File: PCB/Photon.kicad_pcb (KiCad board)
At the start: 2 copper layers, 21.2 x 74.4 mm, 44 parts, among them J1 USB_C_Receptacle_USB2.0_14P, J2 Conn_01x05_Socket, Q1 IRLML6402, Q2 IRLML6402, SW1 TS-1088-AR02016, U1 PY32F002AL15S6TU, U2 TP4056, U3 RT8059GJ5, U4 BCR421UW6-7, U5 DW01A, U6 FS8205A, U7 BCR421UW6-7

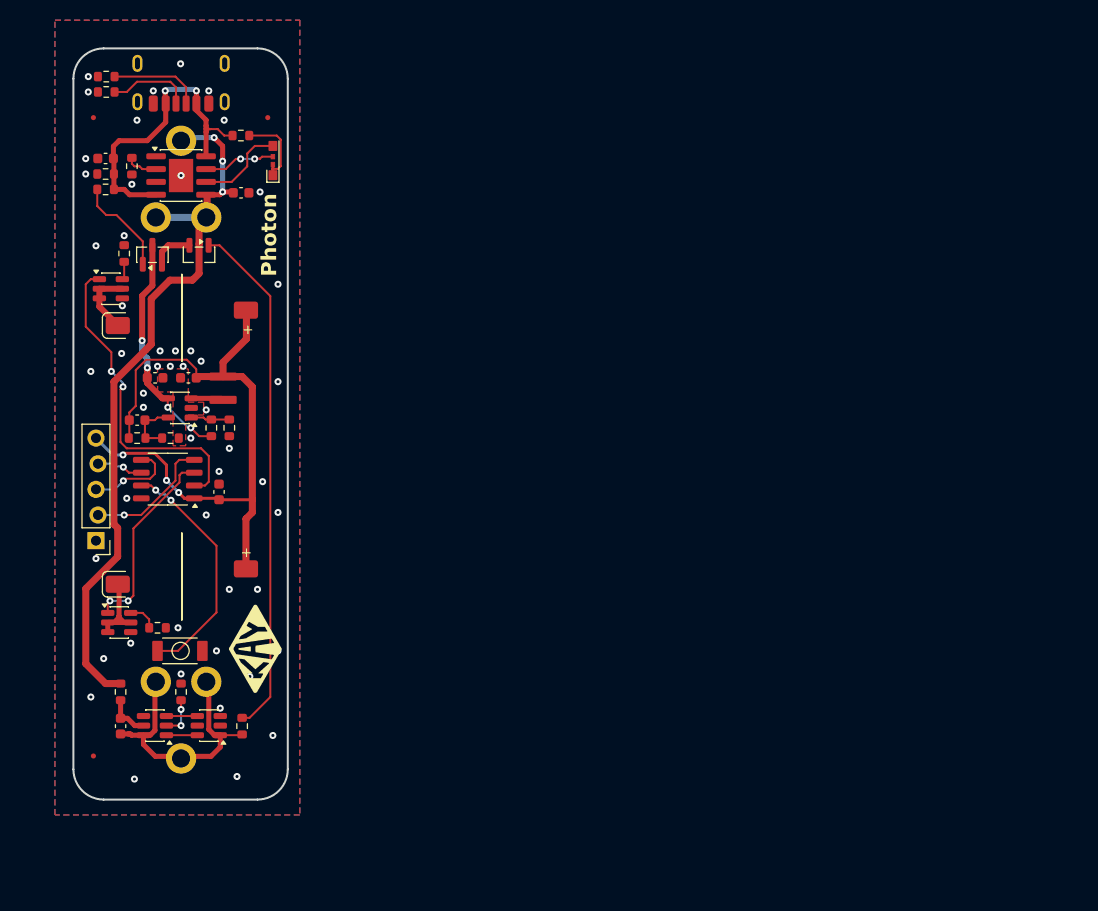
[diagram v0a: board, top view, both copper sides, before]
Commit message: Rotated PCB
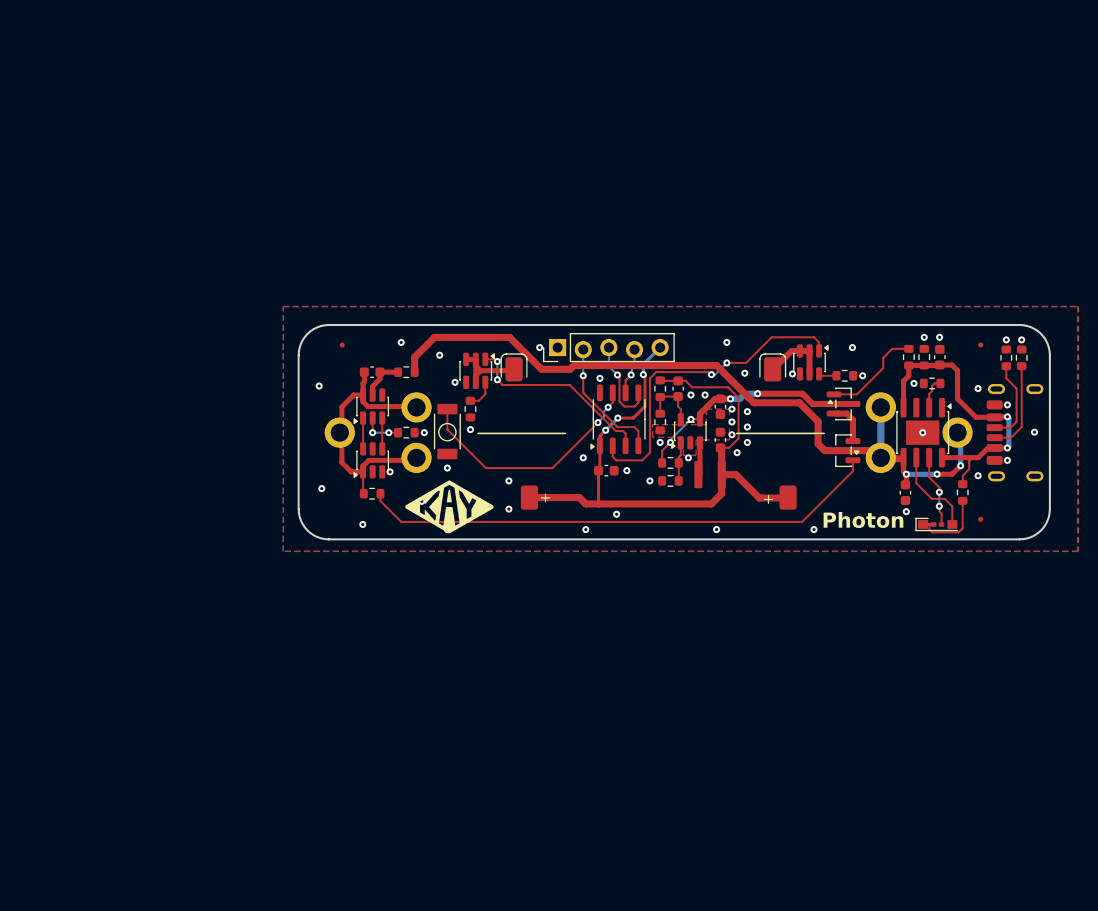
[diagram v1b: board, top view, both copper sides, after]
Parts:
- moved R1 94.9 mm to (136.2, 51.0), turned to 90 degrees
- moved R2 93.0 mm to (134.6, 51.0), turned to 90 degrees
- moved J1 91.1 mm to (136.7, 58.4), turned to 90 degrees
- moved FID3 90.7 mm to (132.1, 49.7), turned to -90 degrees
- moved C3 85.0 mm to (128.0, 50.9), turned to -90 degrees
- moved R5 83.1 mm to (126.5, 50.9), turned to 90 degrees
- moved R10 82.2 mm to (127.3, 53.5), turned to 180 degrees
- moved R4 81.3 mm to (125.0, 50.9), turned to -90 degrees
- moved FID1 81.1 mm to (132.1, 67.0), turned to -90 degrees
- moved BT1 80.1 mm to (125.2, 52.9), turned to 180 degrees
- moved R7 79.8 mm to (130.3, 64.3), turned to -90 degrees
- moved U2 77.8 mm to (126.4, 58.4), turned to -90 degrees
- moved D1 77.1 mm to (129.3, 67.5), turned to 180 degrees
- moved R13 72.4 mm to (118.6, 52.8), turned to 0 degrees
- moved C6 72.2 mm to (124.6, 64.3), turned to 90 degrees
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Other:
- board size 21.2 x 74.4 mm -> 74.4 x 21.2 mm

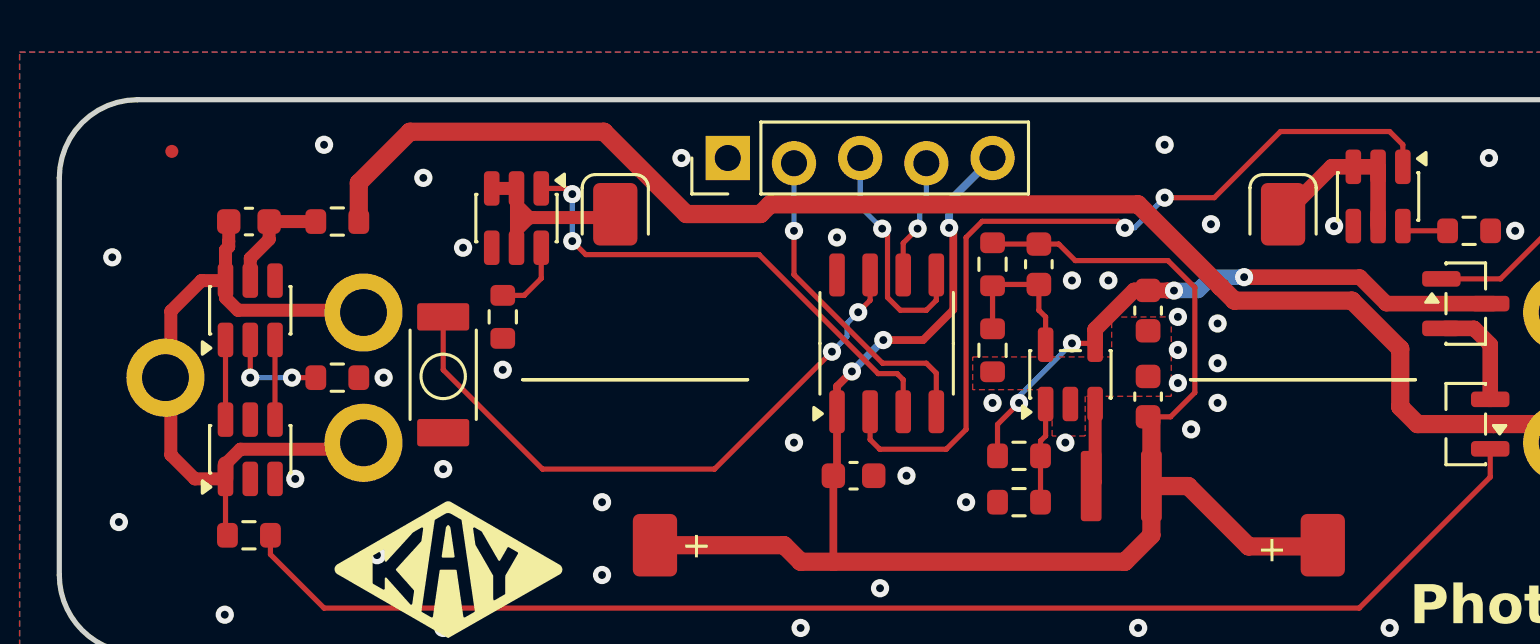
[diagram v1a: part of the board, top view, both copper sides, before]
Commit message: updated debug header and changed resistors for UVLO
Applied teardrop to all vias. some were missing. Thickened trace from neg battery terminal. Updated gerbers
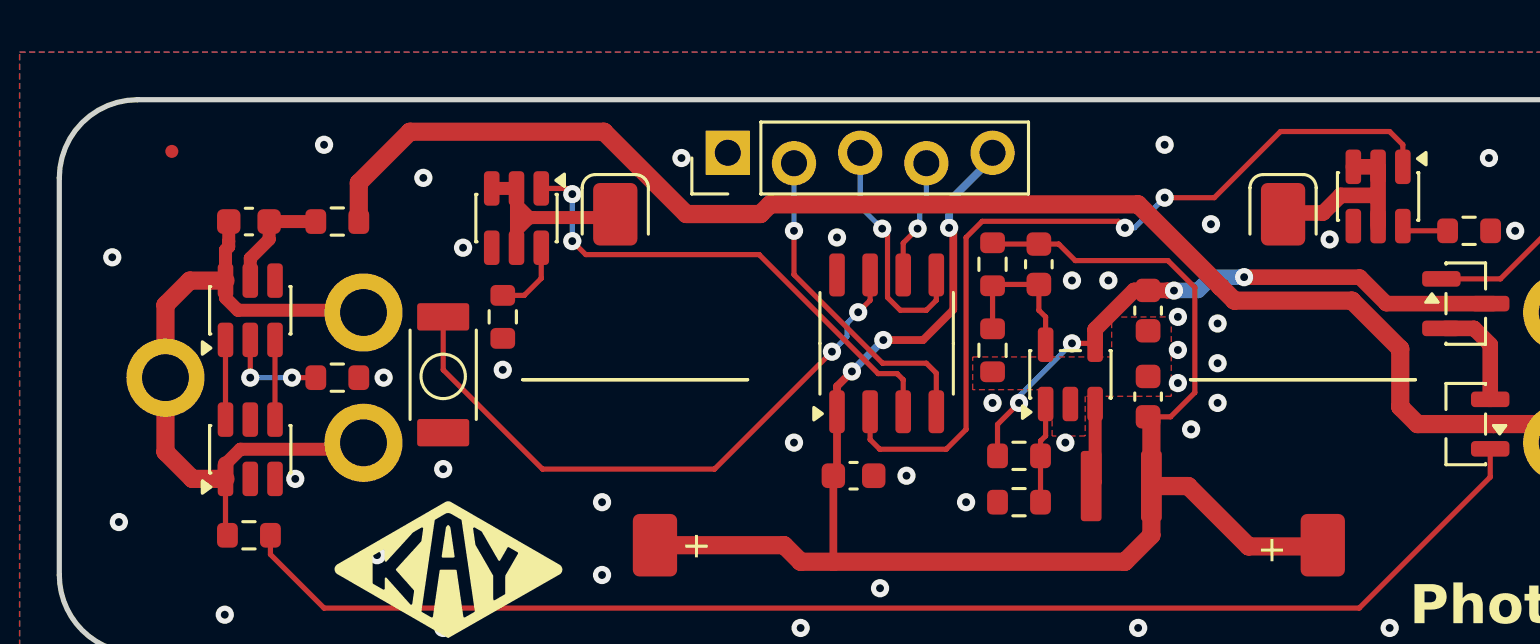
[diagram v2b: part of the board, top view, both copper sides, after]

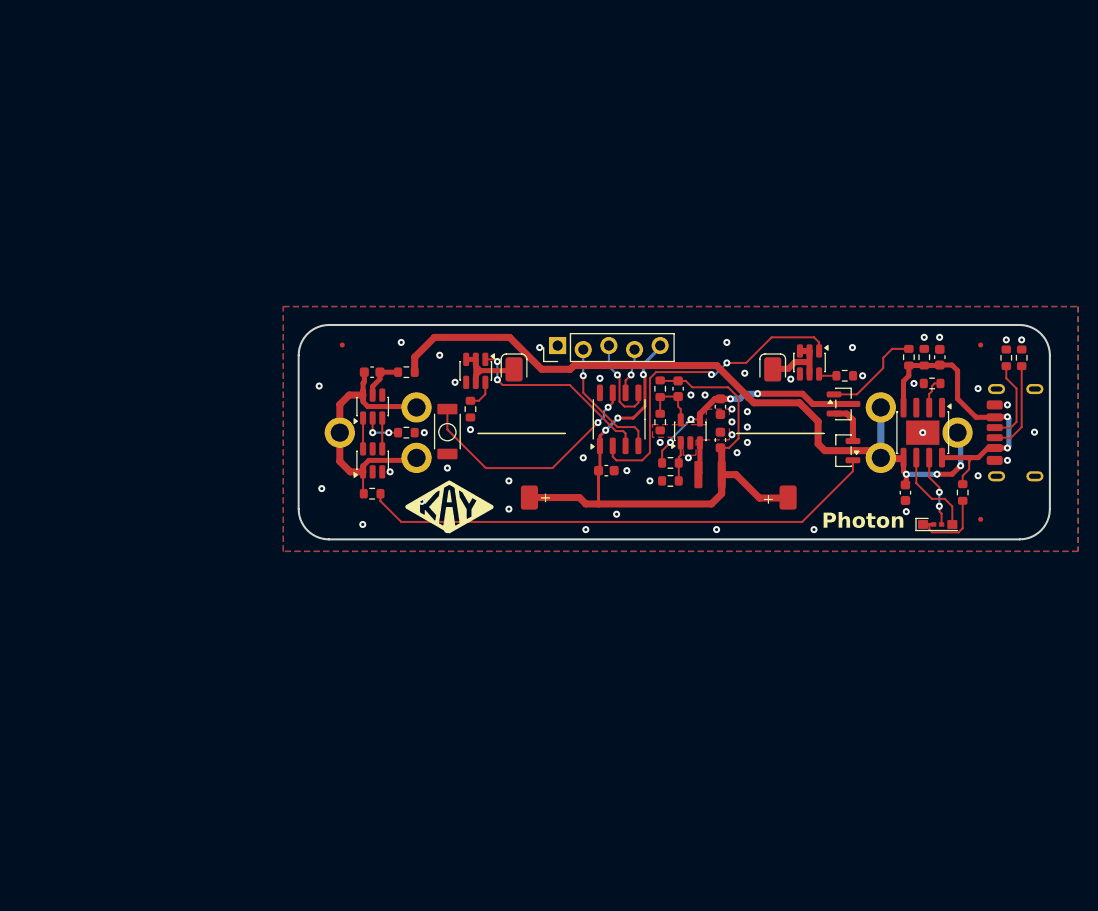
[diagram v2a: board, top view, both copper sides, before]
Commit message: switch to smt32 mcu and cleaned up pcb
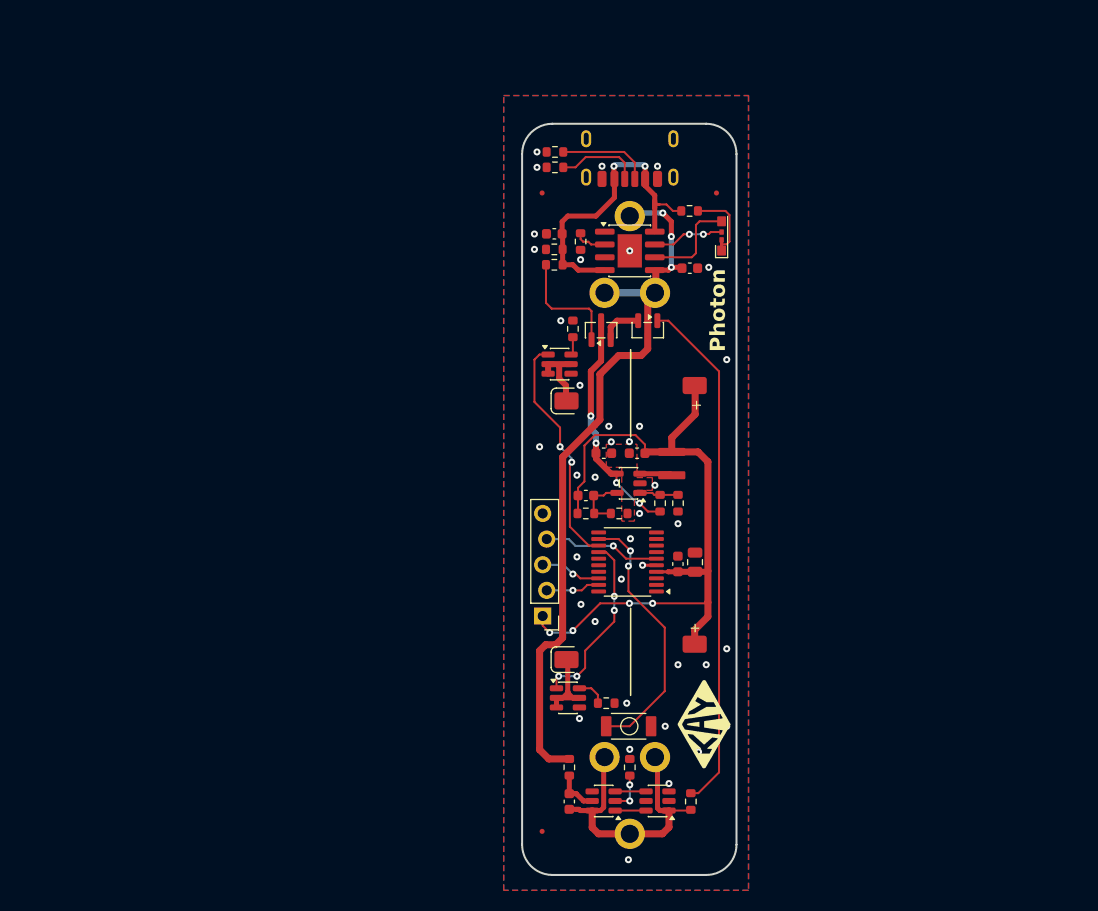
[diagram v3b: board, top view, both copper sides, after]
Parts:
- added C2: 100nF, Capacitor_SMD:C_0603_1608Metric, F.Cu at (102.1, 71.4)
- C1: value 100nF -> 4.7uF; footprint Capacitor_SMD:C_0603_1608Metric -> Capacitor_SMD:C_0805_2012Metric
- J1: value USB_C_Receptacle_USB2.0_14P -> USB_C_Receptacle_USB2.0_6P
- R5: renamed from R3; value 30K -> 12K
- R6: value 100K -> 10K
- U1: value PY32F002AL15S6TU -> STM32G030F6P6TR; footprint Package_SO:SOP-8_3.9x4.9mm_P1.27mm -> Package_SO:TSSOP-20_4.4x6.5mm_P0.65mm
- moved FID2 52.1 mm to (88.7, 97.9), turned to 0 degrees
- moved R1 50.5 mm to (89.9, 30.6), turned to 180 degrees
- moved R2 48.5 mm to (89.9, 32.1), turned to 180 degrees
- moved J1 48.5 mm to (97.3, 30.1), turned to 180 degrees
- moved C8 46.8 mm to (91.3, 94.9), turned to 90 degrees
- moved FID3 46.0 mm to (88.7, 34.6), turned to 0 degrees
- moved U4 45.3 mm to (94.7, 94.9), turned to 180 degrees
- moved U5 44.0 mm to (100.1, 94.9), turned to 180 degrees
- moved R14 43.9 mm to (103.4, 94.9), turned to 90 degrees
- moved R11 42.3 mm to (91.3, 91.5), turned to -90 degrees
- moved FID1 41.6 mm to (105.9, 34.6), turned to 0 degrees
- moved C3 40.1 mm to (89.9, 38.7), turned to 0 degrees
- moved R13 39.9 mm to (97.3, 91.5), turned to -90 degrees
- moved R3 38.9 mm to (103.3, 36.4), turned to 0 degrees
- moved R8 38.2 mm to (89.9, 40.2), turned to 180 degrees
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- renumbered C2 to C4, C6 to C5, C4 to C6, C5 to C7, C7 to C8, R9 to R10, R14 to R11, R13 to R12, R17 to R13, R19 to R14, R16 to R15, R7 to R3, R10 to R4, R4 to R7, R5 to R8, R8 to R9, U5 to U4, U6 to U5, U4 to U6
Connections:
- net /NRST renamed NRST
- J2 pad 1: GND -> +3V3
- J2 pad 2: /SWC -> SWCLK
- J2 pad 3: /SWD -> SWDIO
- J2 pad 5: +3V3 -> GND
- SW1 pad 1: /BTN -> /BUTN
- U1 pad 1: +3V3 -> unconnected-(U1-PB7/PB8-Pad1)
- U1 pad 2: /LED1_EN -> unconnected-(U1-PB9/PC14-Pad2)
- U1 pad 3: /LED2_EN -> unconnected-(U1-PC15-Pad3)
- U1 pad 4: /SWC -> +3V3
- U1 pad 5: /SWD -> GND
- U1 pad 7: /BTN -> unconnected-(U1-PA0-Pad7)
- U1 pad 8: GND -> unconnected-(U1-PA1-Pad8)
- U6 pad 1: /LED1_EN -> LED1_EN
- U7 pad 1: /LED2_EN -> LED2_EN
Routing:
- net /LED1_EN: track 32.3 -> 0.00 mm, vias 2 -> 0
- net /BUTN: track 0.00 -> 26.3 mm, vias 0 -> 2
- net /BTN: track 23.9 -> 0.00 mm, vias 2 -> 0
- net LED1_EN: track 0.00 -> 23.3 mm, vias 0 -> 2
- net /LED2_EN: track 19.3 -> 0.00 mm, vias 2 -> 0
- net LED2_EN: track 0.00 -> 18.1 mm, vias 0 -> 4
- net /SWC: track 12.8 -> 0.00 mm, vias 1 -> 0
- net /SWD: track 8.99 -> 0.00 mm, vias 1 -> 0
- net NRST: track 4.66 -> 11.7 mm
- net +3V3: track 65.0 -> 70.9 mm, vias 3 -> 4
- net SWDIO: track 0.00 -> 5.90 mm, vias 0 -> 1
- net SWCLK: track 0.00 -> 5.37 mm, vias 0 -> 1
- net /DSBL: track 9.26 -> 10.8 mm
- net GND: track 0.00 -> 1.38 mm, vias 51 -> 39
- net /STDBY: track 8.84 -> 9.74 mm
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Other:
- board size 74.4 x 21.2 mm -> 21.2 x 74.4 mm
- board text added: "V6 02-15-2026"
- board text removed: "V5"

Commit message: added gerbers
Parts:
- moved C3 48.1 mm to (42.0, 34.5)
- moved C4 48.1 mm to (46.9, 56.2)
- moved C5 48.1 mm to (55.4, 37.9)
- moved C8 48.1 mm to (43.4, 90.7)
- moved R1 48.1 mm to (42.0, 26.4)
- moved R10 48.1 mm to (48.4, 62.2)
- moved R11 48.1 mm to (43.4, 87.3)
- moved R15 48.1 mm to (47.1, 81.0)
- moved R2 48.1 mm to (42.0, 27.9)
- moved R7 48.1 mm to (42.0, 37.5)
- moved R8 48.1 mm to (42.0, 36.0)
- moved SW1 48.1 mm to (49.4, 83.3)
- moved U5 48.1 mm to (52.2, 90.7)
- moved U6 48.1 mm to (42.5, 47.4)
- moved BT1 48.1 mm to (43.9, 37.3)
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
